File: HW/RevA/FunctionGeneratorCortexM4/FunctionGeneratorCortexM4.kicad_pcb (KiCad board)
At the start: 2 copper layers, 99.1 x 87.6 mm, 74 parts, among them J1 Conn_02x05_Odd_Even, J2 Screw_Terminal_01x02, J3 Conn_02x06_Odd_Even, J4 Conn_01x06, J5 Conn_01x03, J6 Conn_02x04_Odd_Even, J7 Conn_02x07_Odd_Even, Q1 DMG2301L, U1 NCP51460SN33T1G, U10 NCP1729, U11 LTC6910, U12 TL072, U13 TL072, U2 SN74LVC1G3157DCKR, U3 MCP1754S-3302xCB, U4 SN74LVC1G3157DCKR, U6 STM32G474RET

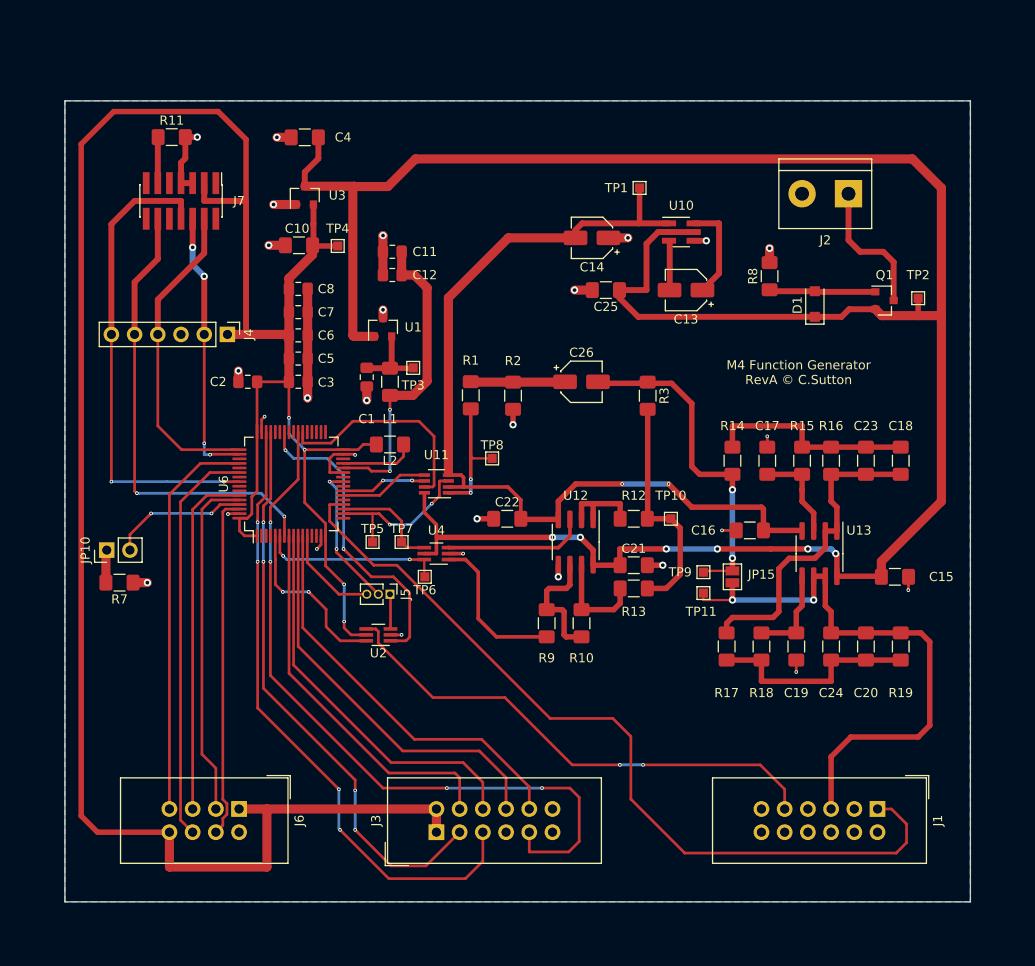
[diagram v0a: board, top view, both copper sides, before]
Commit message: Finished RevA Layout
Dummy STMCubeMX project included in SW dir
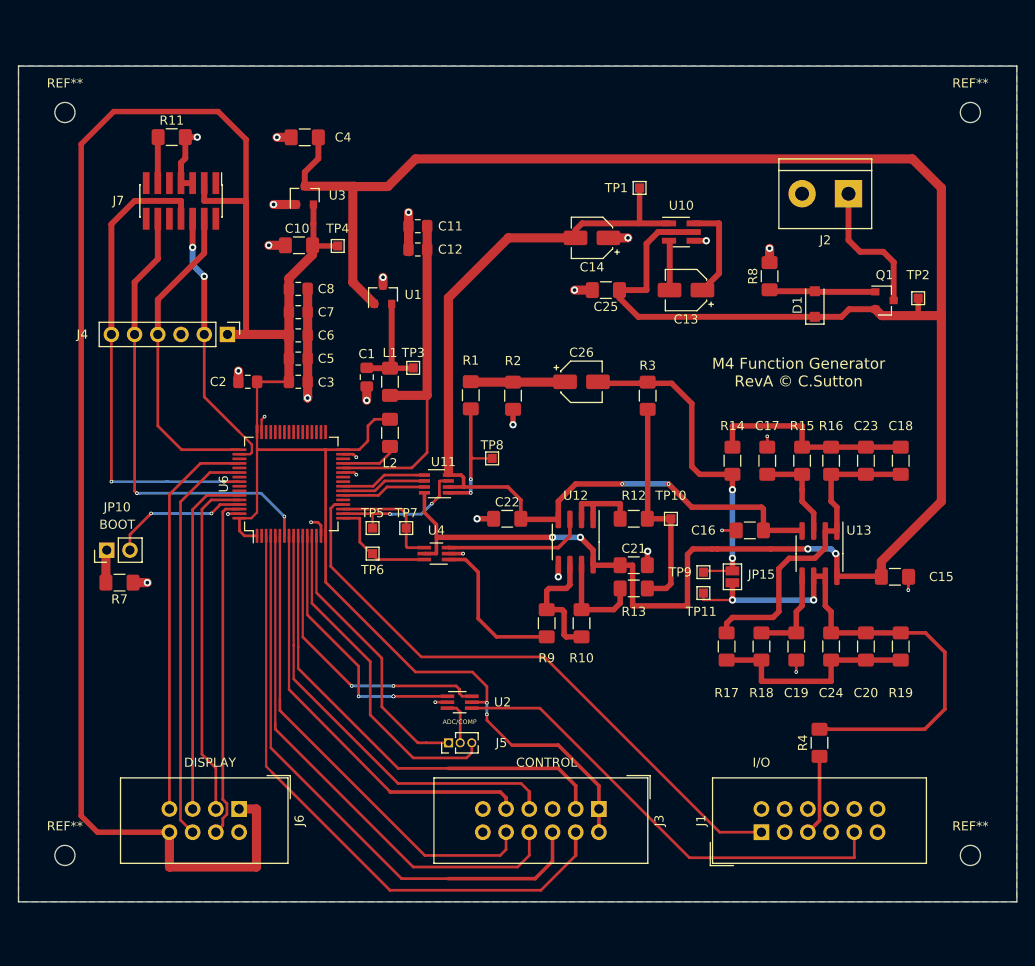
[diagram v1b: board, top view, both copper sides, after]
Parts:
- added R4: 50R, Resistor_SMD:R_1206_3216Metric_Pad1.42x1.75mm_HandSolder, F.Cu at (184.2, 117.2)
- added REF**: MountingHole_2.2mm_M2, MountingHole:MountingHole_2.2mm_M2, F.Cu at (200.7, 129.5)
- added REF**: MountingHole_2.2mm_M2, MountingHole:MountingHole_2.2mm_M2, F.Cu at (101.6, 129.5)
- added REF**: MountingHole_2.2mm_M2, MountingHole:MountingHole_2.2mm_M2, F.Cu at (101.6, 48.3)
- added REF**: MountingHole_2.2mm_M2, MountingHole:MountingHole_2.2mm_M2, F.Cu at (200.7, 48.3)
- moved J3 18.0 mm to (160.0, 124.5), turned to 270 degrees
- moved J5 17.5 mm to (143.6, 117.2), turned to 90 degrees
- moved J1 13.0 mm to (177.8, 127.0), turned to 90 degrees
- moved U2 11.5 mm to (144.8, 112.8), turned to 0 degrees
- moved TP6 6.25 mm to (135.3, 96.5)
- moved C12 3.95 mm to (140.2, 63.2)
- moved C11 3.95 mm to (140.2, 60.7)
- moved U1 3.56 mm to (136.4, 68.2)
- moved TP7 1.61 mm to (138.9, 93.7)
- moved TP5 1.52 mm to (135.3, 93.7)
- moved L2 1.27 mm to (137.2, 83.3), turned to 270 degrees
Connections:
- C20 pad 1: /FUNC_SIG_OUT -> Net-(C20-Pad1)
- C24 pad 1: /FUNC_SIG_OUT -> Net-(C20-Pad1)
- J3 pad 3: /MCU/ENC_A -> /MCU/ENC_SW
- J3 pad 5: /MCU/ENC_B -> GNDS
- J3 pad 7: GNDS -> /MCU/ENC_B
- J3 pad 9: /MCU/ENC_SW -> /MCU/ENC_A
- J5 pad 1: Net-(J5-Pad1) -> /MCU/ADC_IN3
- J5 pad 2: /MCU/COMP1_INP -> Net-(J5-Pad2)
- J5 pad 3: /MCU/ADC_IN1 -> /MCU/COMP1_INP
- JP15 pad 2: /FUNC_SIG_OUT -> Net-(C20-Pad1)
- R19 pad 1: /FUNC_SIG_OUT -> Net-(C20-Pad1)
- TP11 pad 1: /FUNC_SIG_OUT -> Net-(C20-Pad1)
- U13 pad 6: /FUNC_SIG_OUT -> Net-(C20-Pad1)
- U13 pad 7: /FUNC_SIG_OUT -> Net-(C20-Pad1)
- U2 pad 1: /MCU/TIM1_TF1FP1 -> /MCU/TIM2_TF1FP1
- U2 pad 3: Net-(J5-Pad1) -> Net-(J5-Pad2)
- U6 pad 10: /MCU/BTN3 -> /MCU/ENC_SW
- U6 pad 11: /MCU/BTN4 -> /MCU/CH1_MUX
- U6 pad 12: /MCU/ADC_IN1 -> /MCU/TIM2_TF1FP1
- U6 pad 13: Net-(U6-Pad13) -> /MCU/COMP1_INP
- U6 pad 14: Net-(U6-Pad14) -> /MCU/ADC_IN3
- U6 pad 17: Net-(U6-Pad17) -> /AnalogOutput/DCBIAS_INVERT_IN
- U6 pad 22: /AnalogOutput/SG0_IN -> /AnalogOutput/SG2_IN
- U6 pad 24: Net-(U6-Pad24) -> /AnalogOutput/SG0_IN
- U6 pad 25: /MCU/COMP1_INP -> Net-(U6-Pad25)
- U6 pad 3: Net-(U6-Pad3) -> /MCU/BTN1
- U6 pad 38: /AnalogOutput/SG2_IN -> Net-(U6-Pad38)
- U6 pad 39: /MCU/ENC_SW -> Net-(U6-Pad39)
- U6 pad 4: Net-(U6-Pad4) -> /MCU/BTN2
- U6 pad 42: /MCU/TIM1_TF1FP1 -> Net-(U6-Pad42)
- U6 pad 45: /MCU/ENC_A -> Net-(U6-Pad45)
- U6 pad 46: /MCU/ENC_B -> Net-(U6-Pad46)
- U6 pad 5: /MCU/CH1_MUX -> /MCU/BTN3
- U6 pad 6: /AnalogOutput/DCBIAS_INVERT_IN -> /MCU/BTN4
- U6 pad 8: /MCU/BTN1 -> /MCU/ENC_A
- U6 pad 9: /MCU/BTN2 -> /MCU/ENC_B
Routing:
- net Net-(C20-Pad1): track 0.00 -> 61.0 mm, vias 0 -> 2
- net /FUNC_SIG_OUT: track 63.3 -> 9.65 mm, vias 2 -> 0
- net /MCU/TIM1_TF1FP1: track 33.9 -> 0.00 mm, vias 2 -> 0
- net /MCU/ADC_IN3: track 0.00 -> 30.6 mm
- net /MCU/TIM2_TF1FP1: track 0.00 -> 29.6 mm, vias 0 -> 3
- net /MCU/ENC_SW: track 80.1 -> 52.7 mm, vias 4 -> 0
- net /MCU/BTN1: track 41.9 -> 68.8 mm
- net /FUNC_SYNC_OUT: track 91.8 -> 67.0 mm
- net /MCU/ENC_B: track 69.4 -> 48.4 mm, vias 4 -> 0
- net /MCU/BTN2: track 43.1 -> 63.9 mm
- net /MCU/COMP1_INP: track 16.0 -> 36.6 mm, vias 2 -> 0
- net /+3V3: track 271.6 -> 288.7 mm, vias 4 -> 2
- net /MCU/ENC_A: track 62.6 -> 46.7 mm, vias 4 -> 0
- net /AnalogOutput/SG2_IN: track 23.8 -> 9.27 mm
- net /MCU/BTN3: track 44.2 -> 58.2 mm
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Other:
- board size 99.1 x 87.6 mm -> 109.2 x 91.4 mm
- board text added: "ADC/COMP"
- board text added: "BOOT"
- board text added: "CONTROL"
- board text added: "DISPLAY"
- board text added: "I/O"

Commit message: updated RevA
Generated GERBERS
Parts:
- removed U10: NCP1729, Package_TO_SOT_SMD:SOT-23-6_Handsoldering
- added C9: 10uF, Capacitor_SMD:CP_Elec_4x5.7, F.Cu at (161.5, 110.4)
- added D2: LED, LED_SMD:LED_1206_3216Metric_Pad1.42x1.75mm_HandSolder, F.Cu at (191.9, 74.0)
- added D3: LED, LED_SMD:LED_1206_3216Metric_Pad1.42x1.75mm_HandSolder, F.Cu at (160.8, 72.0)
- added D4: LED, LED_SMD:LED_1206_3216Metric_Pad1.42x1.75mm_HandSolder, F.Cu at (126.9, 49.5)
- added R20: 470R, Resistor_SMD:R_1206_3216Metric_Pad1.42x1.75mm_HandSolder, F.Cu at (130.4, 49.5)
- added R21: 50R, Resistor_SMD:R_1206_3216Metric_Pad1.42x1.75mm_HandSolder, F.Cu at (173.2, 117.3)
- added R5: 470R, Resistor_SMD:R_1206_3216Metric_Pad1.42x1.75mm_HandSolder, F.Cu at (194.9, 74.0)
- added R6: 470R, Resistor_SMD:R_1206_3216Metric_Pad1.42x1.75mm_HandSolder, F.Cu at (160.8, 66.2)
- added U5: TC7662Bx0A, Package_SO:SOIC-8_3.9x4.9mm_P1.27mm, F.Cu at (171.2, 61.3)
- added U7: MCP601-xOT, Package_TO_SOT_SMD:SOT-23-5, F.Cu at (168.5, 109.5)
- U3: value MCP1754S-3302xCB -> MCP1703A-3302_SOT223; footprint Package_TO_SOT_SMD:SOT-23 -> Package_TO_SOT_SMD:SOT-223-3_TabPin2
- moved C4 17.6 mm to (145.0, 47.0)
- moved U3 16.6 mm to (144.1, 54.2), turned to 270 degrees
- moved C11 16.5 mm to (139.8, 77.2), turned to 270 degrees
- moved C10 14.9 mm to (133.9, 49.5), turned to 90 degrees
- moved C12 14.2 mm to (142.9, 77.2), turned to 270 degrees
- moved C13 13.3 mm to (171.8, 54.6), turned to 0 degrees
- moved R1 11.2 mm to (156.3, 83.5)
- moved R2 10.5 mm to (160.1, 83.6)
- moved TP4 9.46 mm to (133.9, 53.7), turned to 270 degrees
- moved C14 7.45 mm to (160.4, 54.6), turned to 0 degrees
- moved U11 7.14 mm to (146.7, 83.3)
- moved TP3 6.66 mm to (134.7, 71.8)
- moved TP1 6.59 mm to (160.8, 62.0)
- moved C25 6.29 mm to (165.4, 72.0), turned to 270 degrees
- moved TP8 6.11 mm to (152.8, 81.9)
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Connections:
- U3 pad 1: GNDS -> /+5V
- U3 pad 2: /+3V3 -> GNDS
- U3 pad 3: /+5V -> /+3V3
- U6 pad 20: /FUNC_SYNC_OUT -> /MCU/FUNC1_SYNC
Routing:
- net /FUNC_SYNC_OUT: track 67.0 -> 11.9 mm
- net /MCU/FUNC1_SYNC: track 0.00 -> 42.1 mm
- net /+3V3: track 288.7 -> 312.0 mm
- net Net-(C11-Pad2): track 38.2 -> 22.3 mm
- net /+5V: track 262.5 -> 276.6 mm
- net Net-(R21-Pad2): track 0.00 -> 11.1 mm
- net GNDS: track 65.4 -> 76.3 mm, vias 29 -> 56
- net /MCU/FUNC1_SIG: track 15.6 -> 25.7 mm
- net /AnalogOutput/SG1_IN: track 9.34 -> 18.4 mm
- net /AnalogOutput/SG2_IN: track 9.27 -> 18.2 mm
- net /AnalogOutput/SG0_IN: track 9.40 -> 18.3 mm
- net Net-(C9-Pad1): track 0.00 -> 4.09 mm
- net Net-(D4-Pad2): track 0.00 -> 3.56 mm
- net Net-(D2-Pad2): track 0.00 -> 3.05 mm
- net Net-(R10-Pad2): track 13.5 -> 10.6 mm
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- added copper zone on F.Cu, net GNDS
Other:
- board text added: "3V3"
- board text added: "BYPASS ———>"
- board text added: "GND"
- board text added: "MAX 15V"
- board text added: "RST"
- board text added: "SWCLK"
- board text added: "SWDIO"
- board text added: "SWO"
